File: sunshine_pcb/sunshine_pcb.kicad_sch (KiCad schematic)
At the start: 0 parts

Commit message: Start designing PCB, make the code work (on chan B)
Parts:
- added C1: 220u, Capacitor_THT:CP_Radial_D6.3mm_P2.50mm, symbol Device:C_Polarized_US
- added C2: 10u, Capacitor_SMD:C_1210_3225Metric, symbol Device:C
- added D1: LED, LED_SMD:LED_PLCC_2835, symbol Device:LED
- added J1, J2: XT30PW, Connector_AMASS:AMASS_XT30PW-M_1x02_P2.50mm_Horizontal, symbol custom:XT30PW
- added J3, J4: MR30, Connector_AMASS:AMASS_MR30PW-M_1x03_P3.50mm_Horizontal, symbol Connector_Generic:Conn_01x03
- added J5: USB_C_Receptacle_USB2.0_16P, custom:CONN_GT-USB-7055A_GSW, symbol Connector:USB_C_Receptacle_USB2.0_16P
- added L1: L, custom:L_pol_2016, symbol Device:L
- added SW1: Fingertech, custom:FingertechSwitch, symbol Switch:SW_SPST
- added U1: RP2350_60QFN, Package_DFN_QFN:QFN-60-1EP_7x7mm_P0.4mm_EP3.4x3.4mm, symbol MCU_RaspberryPi_RP2350:RP2350_60QFN
- added U2: W25Q128JVP, Package_SON:WSON-8-1EP_6x5mm_P1.27mm_EP3.4x4.3mm, symbol Memory_Flash:W25Q128JVP
- added U3: LIS3MDL, Package_LGA:LGA-12_2x2mm_P0.5mm, symbol Sensor_Magnetic:LIS3MDL
- added U4: ADXL375, Package_LGA:LGA-14_3x5mm_P0.8mm_LayoutBorder1x6y, symbol Sensor_Motion:ADXL343
- added U5: HT7533, PCM_JLCPCB:SOT-89-3_L4.5-W2.5-P1.50-LS4.2-BR, symbol PCM_JLCPCB-Power:LDO, 3.3V, 0.1A
- added U6: FS2A, custom:FS2A, symbol custom:FS2A
- added U7: DualAM32, custom:DualAM32, symbol custom:DualAM32
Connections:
- new net: J5.A1 (GND), J5.A12 (GND), J5.B1 (GND), J5.B12 (GND)
- new net: J5.A4 (VBUS), J5.A9 (VBUS), J5.B4 (VBUS), J5.B9 (VBUS)
- new net: U4.2 (GND), U4.4 (GND), U4.5 (GND)
- new net: U3.12 (GND), U3.2 (GND), U3.3 (GND)
- new net GND: U7.12 (GND), U7.8 (GND)
- new net S1: U7.9 (S1)
- new net S2: U7.10 (S2)
- new net VDC: U7.7 (+VDC)

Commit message: Do layout
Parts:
- removed J1, J2: XT30PW, Connector_AMASS:AMASS_XT30PW-M_1x02_P2.50mm_Horizontal, symbol custom:XT30PW
- added C10, C11, C13, C14, C15, C16, C17, C18, C19, C22, C25, C26, C27, C28, C30: 100nF, PCM_JLCPCB:C_0402, symbol PCM_JLCPCB-Capacitors:0402,100nF,(2)
- added C12, C29, C7, C8, C9: 4.7uF, PCM_JLCPCB:C_0402, symbol PCM_JLCPCB-Capacitors:0402,4.7uF
- added C23, C24: 15pF, PCM_JLCPCB:C_0402, symbol PCM_JLCPCB-Capacitors:0402,15pF
- added C3, C4: 10u, Capacitor_SMD:C_1210_3225Metric, symbol Device:C
- added C5, C6: 10uF, PCM_JLCPCB:C_0805, symbol PCM_JLCPCB-Capacitors:0805,10uF,(2)
- added D2, D3: 1N5819WS, PCM_JLCPCB:D_SOD-323, symbol PCM_JLCPCB-Diodes:Schottky,1N5819WS
- added D4, D5, D6: LED, LED_SMD:LED_PLCC_2835, symbol Device:LED
- added D7: SMF12A, PCM_JLCPCB:D_SOD-123FL, symbol PCM_JLCPCB-Diodes:TVS-Uni,SMF12A
- added J1, J2: Soldered, Connector_Wire:SolderWire-0.5sqmm_1x02_P4.6mm_D0.9mm_OD2.1mm_Relief, symbol Connector_Generic:Conn_01x02
- added Q1: AO3401A, PCM_JLCPCB:Q_SOT-23, symbol PCM_JLCPCB-Transistors:PMOS,AO3401A
- added R1, R15, R16, R17, R19, R2, R3: 5.1kΩ, PCM_JLCPCB:R_0402, symbol PCM_JLCPCB-Resistors:0402,5.1kΩ
- added R10, R12, R13, R14: 33Ω, PCM_JLCPCB:R_0805, symbol PCM_JLCPCB-Resistors:0805,33Ω
- added R11, R18, R7, R8, R9: 1kΩ, PCM_JLCPCB:R_0402, symbol PCM_JLCPCB-Resistors:0402,1kΩ
- added R4, R5, R6: 33Ω, PCM_JLCPCB:R_0402, symbol PCM_JLCPCB-Resistors:0402,33Ω
- added S1, S2: TS-1187A-C-B-B, PCM_JLCPCB:SW-SMD_4P-L5.1-W5.1-P3.70-LS6.5-TL-2, symbol PCM_JLCPCB-Connectors_Buttons:Tactile Button, 160gf, 12V, 50mA, 5.1mm
- added U8: USBLC6-2P6, Package_TO_SOT_SMD:SOT-666, symbol Power_Protection:USBLC6-2P6
- added Y1: ABM8-272-T3, Crystal:Crystal_SMD_3225-4Pin_3.2x2.5mm, symbol Device:Crystal_GND24
- J3, J4: value MR30 -> Soldered; footprint Connector_AMASS:AMASS_MR30PW-M_1x03_P3.50mm_Horizontal -> Connector_Wire:SolderWire-0.5sqmm_1x03_P4.6mm_D0.9mm_OD2.1mm_Relief; LCSC C19268036 -> C503478
- J5: value USB_C_Receptacle_USB2.0_16P -> VerticalUSB
- L1: value L -> 3.3u
- U1: footprint Package_DFN_QFN:QFN-60-1EP_7x7mm_P0.4mm_EP3.4x3.4mm -> Package_DFN_QFN:QFN-60-1EP_7x7mm_P0.4mm_EP3.4x3.4mm_ThermalVias
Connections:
- net GND: now also C1.2, C2.2, D1.1 (K), J5.A1 (GND), J5.A12 (GND), J5.B1 (GND), J5.B12 (GND), U1.47 (VREG_PGND), U1.61 (GND), U2.4 (GND), U2.9 (EP), U3.12 (GND), U3.2 (GND), U3.3 (GND), U4.2 (GND), U4.4 (GND), U4.5 (GND), U5.1 (GND), U6.6 (GND), C10.2, C11.2, C12.2, C13.2, C14.2, C15.2, C16.2, C17.2, C18.2, C19.2, C22.2, C23.1, C24.1, C25.2, C26.2, C27.2, C28.2, C29.2, C3.2, C30.2, C4.2, C5.2, C6.2, C7.2, C8.2, C9.2, D4.1 (K), D5.1 (K), D6.1 (K), D7.2, J2.2 (Pin_2), R1.2, R18.2, R2.2, R3.1, S1.3 (C), S1.4 (D), S2.3 (C), S2.4 (D), U8.2 (GND), Y1.2, Y1.4
- net S1: now also U1.9 (GPIO6)
- net S2: now also U1.12 (GPIO8)
- net VDC: now also C1.1, C2.1, SW1.2 (B), C3.1, C4.1, D7.1, R16.1
- net at U7.1 (M1A): now also J3.3 (Pin_3)
- net at U7.11 (+5V): now also D2.2
- net at U7.2 (M1B): now also J3.2 (Pin_2)
- net at U7.3 (M1C): now also J3.1 (Pin_1)
- net at U7.4 (M2A): now also J4.1 (Pin_1)
- net at U7.5 (M2B): now also J4.2 (Pin_2)
- net at U7.6 (M2C): now also J4.3 (Pin_3)
- net BATT1_+: now reaches SW1.1 (A)
- net BATT1_+: now also J1.1 (Pin_1)
- net VBUS: now reaches J5.A4 (VBUS), J5.A9 (VBUS), J5.B4 (VBUS), J5.B9 (VBUS)
- net VBUS: now also D3.2, U8.5 (VBUS)
- net at J5.A5 (CC1): now also R1.1
- net USB_C_D+: now reaches J5.A6 (D+)
- net USB_C_D+: now also J5.B6 (D+), U8.3 (I/O2)
- net USB_C_D-: now reaches J5.A7 (D-)
- net USB_C_D-: now also J5.B7 (D-), U8.1 (I/O1)
- net at J5.B5 (CC2): now also R2.1
- net at J5.S1 (SHIELD): now also R3.2
- net QSPI_SS: now reaches U2.1 (~{CS})
- net QSPI_SS: now also U1.60 (QSPI_SS), R7.1
- net QSPI_SD1: now reaches U2.2 (DO/IO_{1})
- net QSPI_SD1: now also U1.59 (QSPI_SD1)
- net QSPI_SD2: now reaches U2.3 (~{WP}/IO_{2})
- net QSPI_SD2: now also U1.58 (QSPI_SD2)
- net QSPI_SD0: now reaches U2.5 (DI/IO_{0})
- net QSPI_SD0: now also U1.57 (QSPI_SD0)
- net QSPI_SCK: now reaches U2.6 (CLK)
- net QSPI_SCK: now also U1.56 (QSPI_SCLK)
- net QSPI_SD3: now reaches U2.7 (~{HOLD}/~{RESET}/IO_{3})
- net QSPI_SD3: now also U1.55 (QSPI_SD3)
- net +3V3: now reaches U2.8 (VCC)
- net +3V3: now also U1.1 (IOVDD), U1.11 (IOVDD), U1.20 (IOVDD), U1.30 (IOVDD), U1.38 (IOVDD), U1.44 (ADC_AVDD), U1.45 (IOVDD), U1.49 (VREG_VIN), U1.53 (USB_OTP_VDD), U1.54 (QSPI_IOVDD), U3.5 (Vdd), U3.6 (Vdd_IO), U4.1 (Vdd_I/O), U4.6 (Vs), U5.3 (VOUT), C13.1, C14.1, C15.1, C16.1, C17.1, C18.1, C19.1, C22.1, C25.1, C26.1, C28.1, C29.1, C6.1, C8.1, R4.1
- net at D1.2 (A): now also R10.2
- net +5V: now reaches U5.2 (VIN)
- net +5V: now also U6.5 (+5V), C5.1, D2.1, D3.1, Q1.2 (S), R19.1
- net IMU_MISO: now reaches U4.12 (SDO/ADDR)
- net IMU_MISO: now also U1.16 (GPIO12)
- net IMU_MOSI: now reaches U4.13 (SDA/SDI/SDIO)
- net IMU_MOSI: now also U1.15 (GPIO11)
- net IMU_SCK: now reaches U4.14 (SCL/SCLK)
- net IMU_SCK: now also U1.14 (GPIO10)
- net IMU_CS: now reaches U4.7 (~{CS})
- net IMU_CS: now also U1.17 (GPIO13)
- net IMU_INT1: now reaches U4.8 (INT1)
- net IMU_INT1: now also U1.18 (GPIO14)
- net IMU_INT2: now reaches U4.9 (INT2)
- net IMU_INT2: now also U1.19 (GPIO15)
- net R1: now reaches U6.1
- net R1: now also U1.3 (GPIO1)
- net R2: now reaches U6.2
- net R2: now also U1.5 (GPIO3)
- net R3: now reaches U6.3
- net R3: now also U1.8 (GPIO5)
- net R4: now reaches U6.4
- net R4: now also U1.10 (GPIO7)
- net +1V1: now reaches L1.1
- net +1V1: now also U1.23 (DVDD), U1.39 (DVDD), U1.50 (VREG_FB), U1.6 (DVDD), C10.1, C11.1, C12.1, C9.1
- net VREG_LX: now reaches L1.2
- net VREG_LX: now also U1.48 (VREG_LX)
- net LED: now reaches U1.13 (GPIO9)
- net LED: now also R11.1
- net at U1.21 (XIN): now also C23.2, Y1.3
- net at U1.22 (XOUT): now also R8.2
- net RESET: now reaches U1.26 (RUN)
- net RESET: now also R9.1
- net MAG_MISO: now reaches U1.27 (GPIO16)
- net MAG_MISO: now also U3.9 (SDO/SA1)
- net MAG_CS: now reaches U1.28 (GPIO17)
- net MAG_CS: now also U3.10 (~{CS})
- net MAG_SCK: now reaches U1.29 (GPIO18)
- net MAG_SCK: now also U3.1 (SCL/SPC)
- net MAG_MOSI: now reaches U1.31 (GPIO19)
- net MAG_MOSI: now also U3.11 (SDA/SDI/SDO)
- net MAG_DRDY: now reaches U1.32 (GPIO20)
- net MAG_DRDY: now also U3.8 (DRDY)
- net MAG_INT: now reaches U1.33 (GPIO21)
- net MAG_INT: now also U3.7 (INT)
- net at U1.40 (GPIO26_ADC0): now also C30.1, R15.2, R17.1
- net VREG_AVDD: now reaches U1.46 (VREG_AVDD)
- net VREG_AVDD: now also C7.1, R4.2
- net at U1.51 (USB_DM): now also R6.1
- net at U1.52 (USB_DP): now also R5.1
- net at U3.4 (C1): now also C27.1
- new net: R15.1, R16.2
- new net: C24.2, R8.1, Y1.1
- new net: Q1.3 (D), R10.1, R12.1, R13.1, R14.1
- new net: D6.2 (A), R14.2
- new net: Q1.1 (G), R11.2, R19.2
- new net: D4.2 (A), R12.2
- new net: R9.2, S2.1 (A), S2.2 (B)
- new net: R17.2, R18.1
- new net: R7.2, S1.1 (A), S1.2 (B)
- new net: D5.2 (A), R13.2
- new net BATT2_+: J1.2 (Pin_2), J2.1 (Pin_1)
- new net USB_D+: R5.2, U8.4 (I/O2)
- new net USB_D-: R6.2, U8.6 (I/O1)
- no-connect marks 0 -> 16
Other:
- moved on the sheet: C1, C2, D1, J3, J4, J5, L1, SW1, U1, U2, U3, U4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

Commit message: Add some protection
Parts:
- added D10, D8, D9: SMF5.0A, PCM_JLCPCB:D_SOD-123FL, symbol PCM_JLCPCB-Diodes:TVS-Uni,SMF5.0A
- added R20, R21: 1kΩ, PCM_JLCPCB:R_0402, symbol PCM_JLCPCB-Resistors:0402,1kΩ
- J1, J2: footprint Connector_Wire:SolderWire-0.5sqmm_1x02_P4.6mm_D0.9mm_OD2.1mm_Relief -> Connector_Wire:SolderWire-0.75sqmm_1x02_P4.8mm_D1.25mm_OD2.3mm_Relief
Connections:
- net +5V: now also D8.1
- net GND: now also D10.2, D8.2, D9.2
- net S1: now also R20.1; no longer U7.9 (S1)
- net S2: now also R21.1; no longer U7.10 (S2)
- new net S1_C: D10.1, R20.2, U7.9 (S1)
- new net S2_C: D9.1, R21.2, U7.10 (S2)
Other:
- moved on the sheet: C1, C2, C3, C4, D2, J3, J4, U7

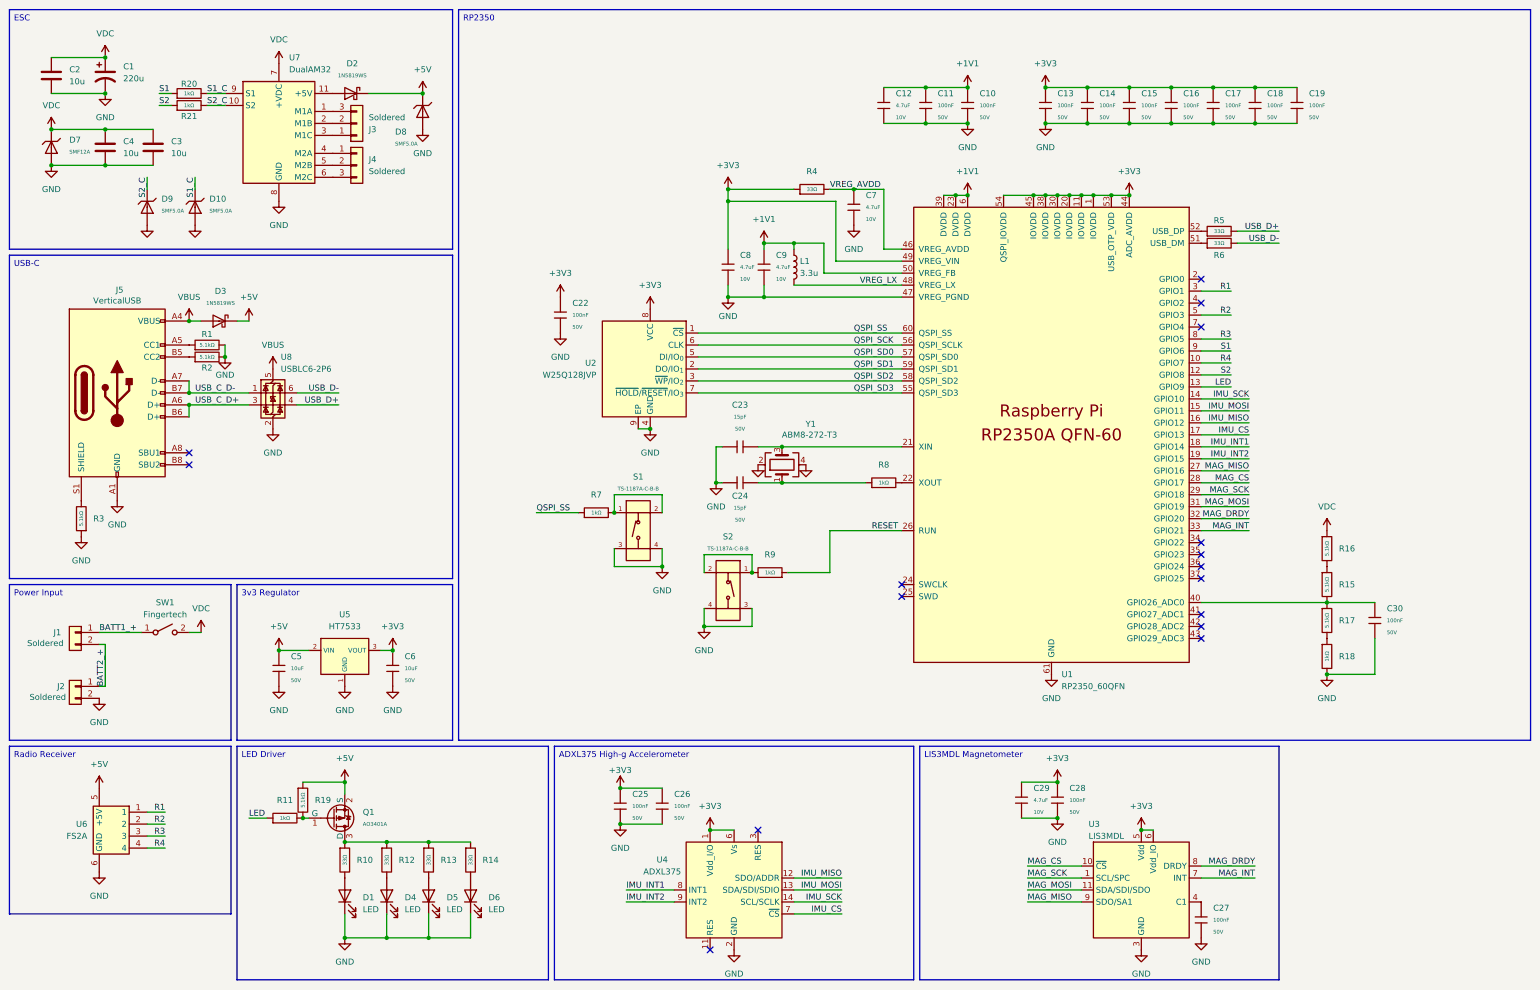
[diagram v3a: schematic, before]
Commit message: Re-do schematic for ESP32
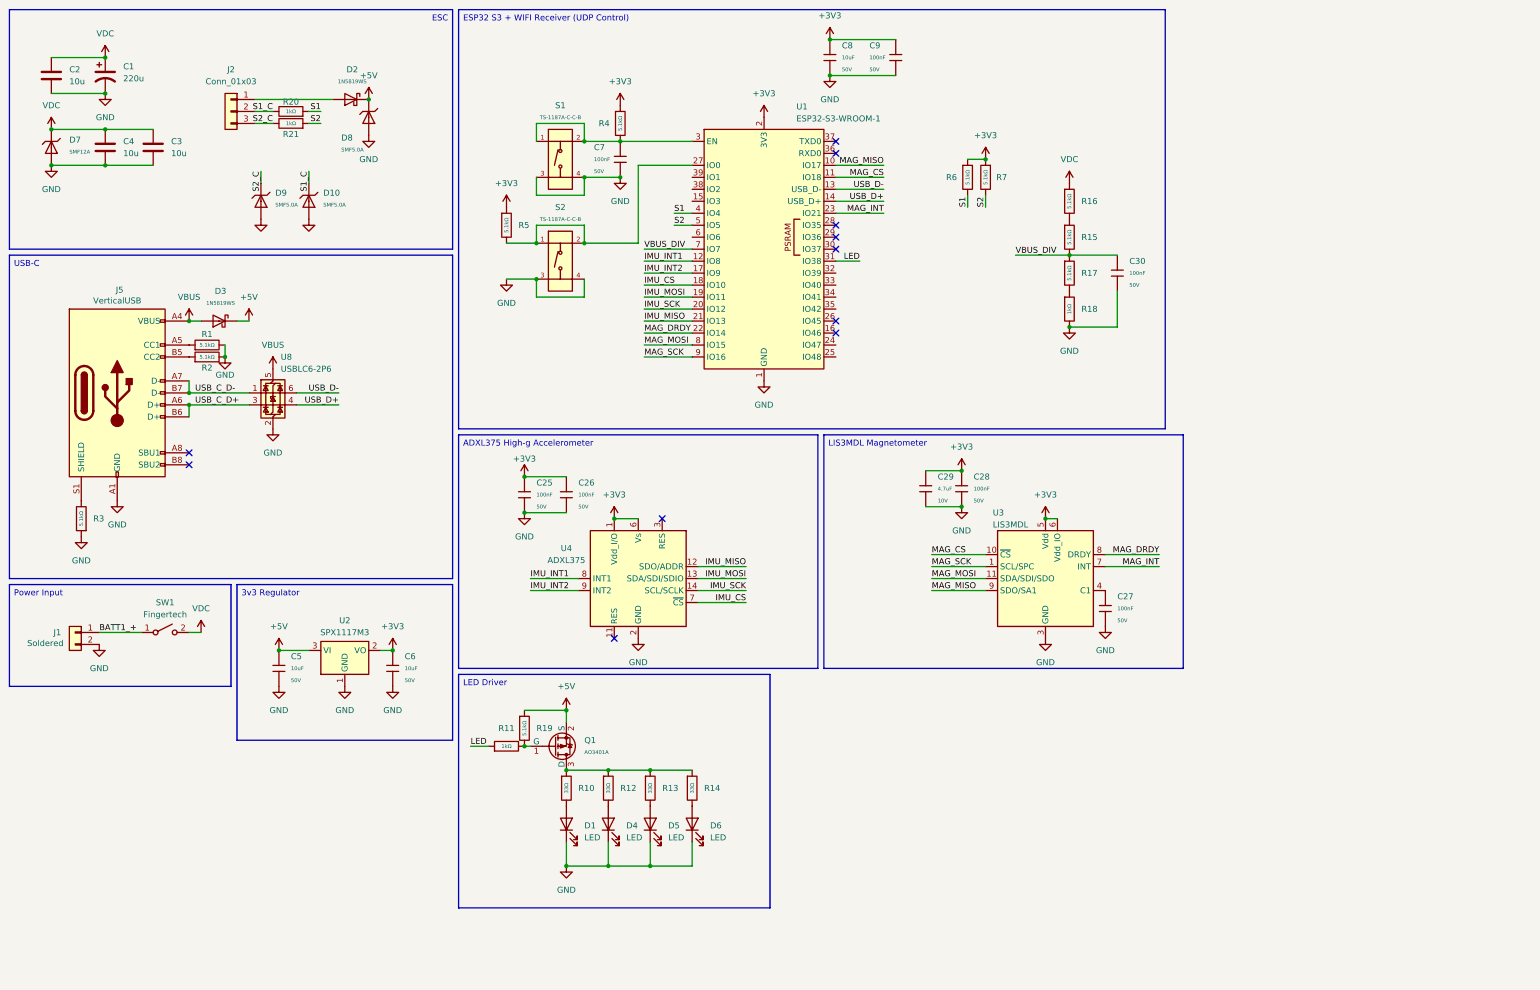
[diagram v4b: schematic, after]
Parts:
- removed C10, C11, C13, C14, C15, C16, C17, C18, C19, C22: 100nF, PCM_JLCPCB:C_0402, symbol PCM_JLCPCB-Capacitors:0402,100nF,(2)
- removed C12, C7, C8, C9: 4.7uF, PCM_JLCPCB:C_0402, symbol PCM_JLCPCB-Capacitors:0402,4.7uF
- removed C23, C24: 15pF, PCM_JLCPCB:C_0402, symbol PCM_JLCPCB-Capacitors:0402,15pF
- removed J2: Soldered, Connector_Wire:SolderWire-0.75sqmm_1x02_P4.8mm_D1.25mm_OD2.3mm_Relief, symbol Connector_Generic:Conn_01x02
- removed J3, J4: Soldered, Connector_Wire:SolderWire-0.5sqmm_1x03_P4.6mm_D0.9mm_OD2.1mm_Relief, symbol Connector_Generic:Conn_01x03
- removed L1: 3.3u, custom:L_pol_2016, symbol Device:L
- removed R4, R5, R6: 33Ω, PCM_JLCPCB:R_0402, symbol PCM_JLCPCB-Resistors:0402,33Ω
- removed R7, R8, R9: 1kΩ, PCM_JLCPCB:R_0402, symbol PCM_JLCPCB-Resistors:0402,1kΩ
- removed U1: RP2350_60QFN, Package_DFN_QFN:QFN-60-1EP_7x7mm_P0.4mm_EP3.4x3.4mm_ThermalVias, symbol MCU_RaspberryPi_RP2350:RP2350_60QFN
- removed U2: W25Q128JVP, Package_SON:WSON-8-1EP_6x5mm_P1.27mm_EP3.4x4.3mm, symbol Memory_Flash:W25Q128JVP
- removed U5: HT7533, PCM_JLCPCB:SOT-89-3_L4.5-W2.5-P1.50-LS4.2-BR, symbol PCM_JLCPCB-Power:LDO, 3.3V, 0.1A
- removed U6: FS2A, custom:FS2A, symbol custom:FS2A
- removed U7: DualAM32, custom:DualAM32, symbol custom:DualAM32
- removed Y1: ABM8-272-T3, Crystal:Crystal_SMD_3225-4Pin_3.2x2.5mm, symbol Device:Crystal_GND24
- added C7, C9: 100nF, PCM_JLCPCB:C_0402, symbol PCM_JLCPCB-Capacitors:0402,100nF,(2)
- added C8: 10uF, PCM_JLCPCB:C_0805, symbol PCM_JLCPCB-Capacitors:0805,10uF,(2)
- added J2: Conn_01x03, Connector_Wire:SolderWire-0.25sqmm_1x03_P4.5mm_D0.65mm_OD2mm, symbol Connector_Generic:Conn_01x03
- added R4, R5, R6, R7: 5.1kΩ, PCM_JLCPCB:R_0402, symbol PCM_JLCPCB-Resistors:0402,5.1kΩ
- added U1: ESP32-S3-WROOM-1, RF_Module:ESP32-S3-WROOM-1, symbol RF_Module:ESP32-S3-WROOM-1
- added U2: SPX1117M3, Package_TO_SOT_SMD:SOT-223-3_TabPin2, symbol Regulator_Linear:AMS1117-3.3
- S1, S2: value TS-1187A-C-B-B -> TS-1187A-C-C-B; Part TS-1187A-C-B-B -> TS-1187A-B-A-B
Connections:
- net BATT2_+ is gone; now on net GND: J1.2 (Pin_2)
- net +3V3: now also C8.1, C9.1, R4.1, R5.1, R6.1, R7.1, U1.2 (3V3), U2.2 (VO)
- net +5V: now also U2.3 (VI)
- net GND: now also C7.2, C8.2, C9.2, U1.1 (GND), U1.40 (GND), U1.41 (GND), U2.1 (GND)
- net IMU_CS: now also U1.18 (IO10)
- net IMU_INT1: now also U1.12 (IO8)
- net IMU_INT2: now also U1.17 (IO9)
- net IMU_MISO: now also U1.21 (IO13)
- net IMU_MOSI: now also U1.19 (IO11)
- net IMU_SCK: now also U1.20 (IO12)
- net LED: now also U1.31 (IO38)
- net MAG_CS: now also U1.11 (IO18)
- net MAG_DRDY: now also U1.22 (IO14)
- net MAG_INT: now also U1.23 (IO21)
- net MAG_MISO: now also U1.10 (IO17)
- net MAG_MOSI: now also U1.8 (IO15)
- net MAG_SCK: now also U1.9 (IO16)
- net S1: now also R6.2, U1.4 (IO4)
- net S1_C: now also J2.2 (Pin_2)
- net S2: now also R7.2, U1.5 (IO5)
- net S2_C: now also J2.3 (Pin_3)
- net USB_D+: now also U1.14 (USB_D+)
- net USB_D-: now also U1.13 (USB_D-)
- net at D2.2: now also J2.1 (Pin_1)
- net VBUS_DIV: now reaches C30.1, R15.2, R17.1
- net VBUS_DIV: now also U1.7 (IO7)
- net at S2.1 (A), S2.2 (B): now also R5.2, U1.27 (IO0)
- net at S1.1 (A), S1.2 (B): now also C7.1, R4.2, U1.3 (EN)
- no-connect marks 16 -> 11
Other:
- moved on the sheet: C25, C26, C27, C28, C29, C30, D1, D10, D2, D4, D5, D6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
